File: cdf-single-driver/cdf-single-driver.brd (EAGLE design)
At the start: 48.3 x 40.6 mm, 30 parts, among them IC1 R-789.0-0.5, IC2 UCC27423

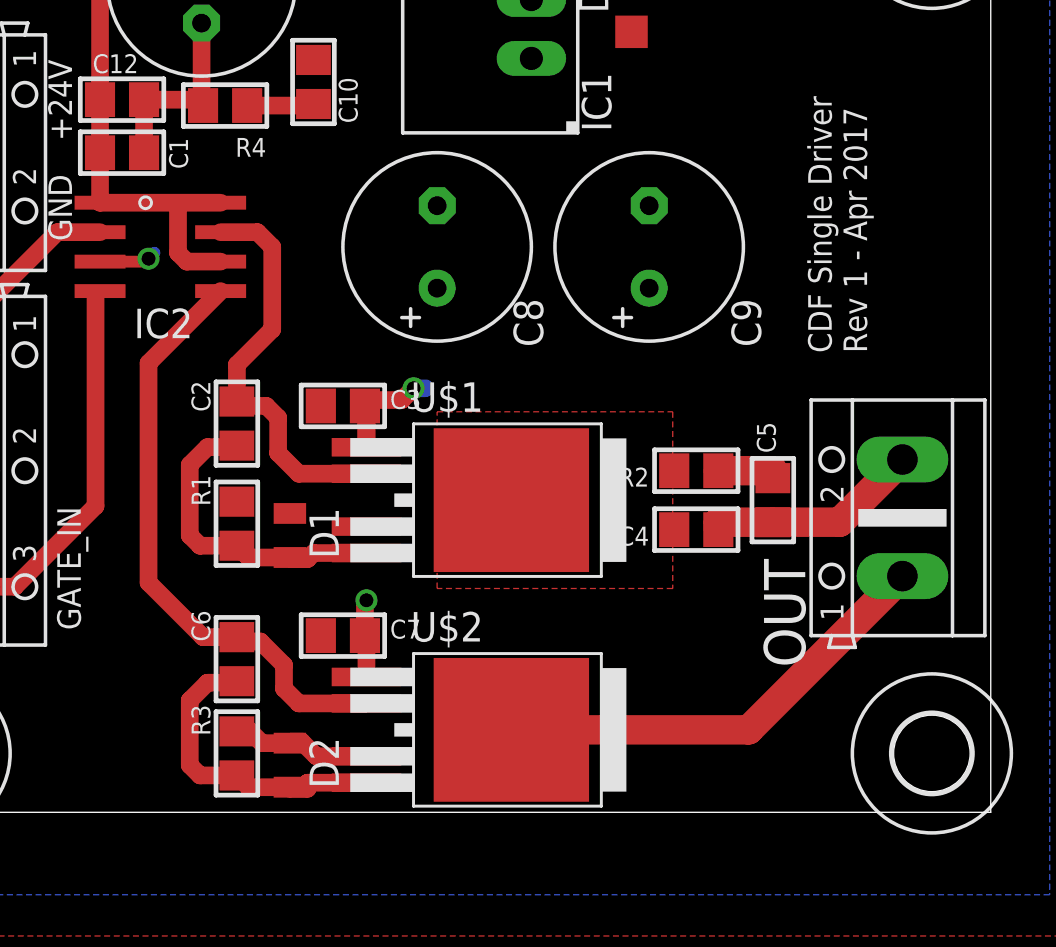
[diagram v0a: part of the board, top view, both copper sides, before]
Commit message: small cdf-single-driver changes
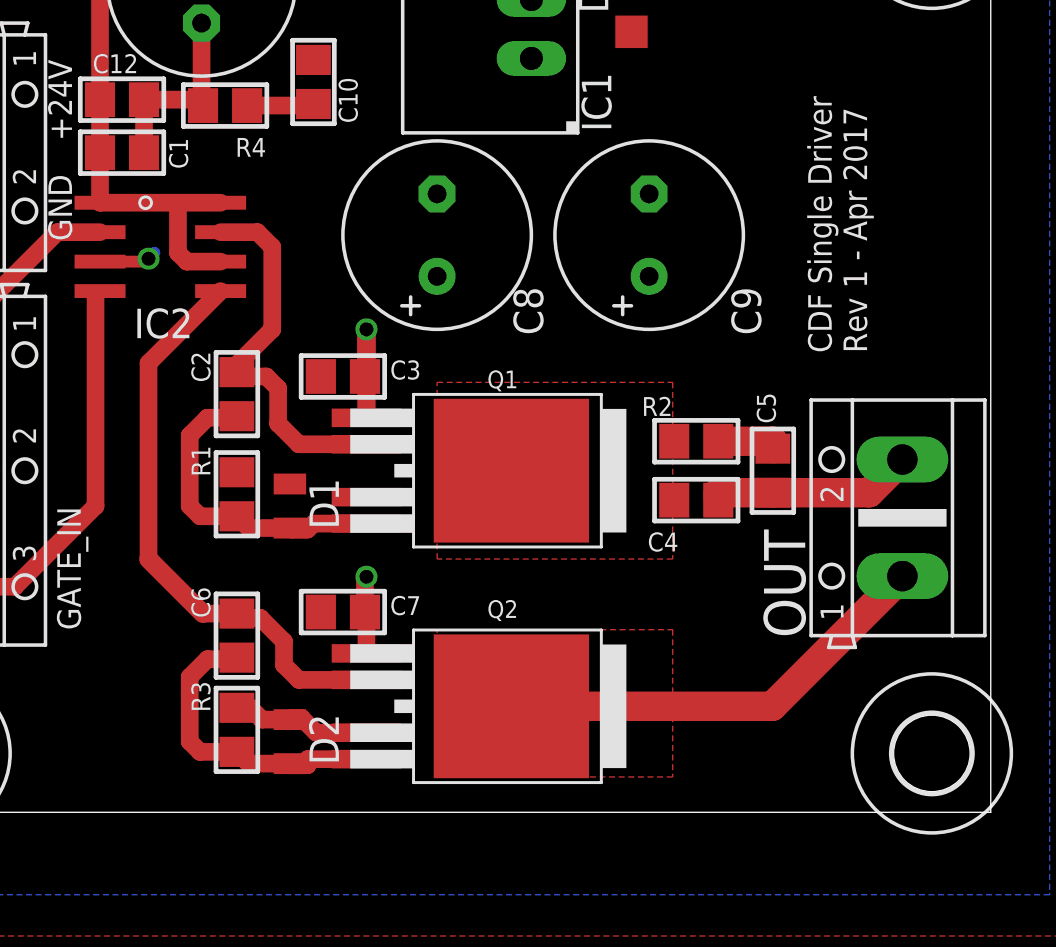
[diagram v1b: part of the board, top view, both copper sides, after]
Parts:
- removed U$1, U$2: FDD8424H, keves:TO252-4
- added Q1, Q2: FDD8424H, keves:TO252-4
- moved C2 1.27 mm to (15.7, 18.0)
- moved C3 1.27 mm to (20.3, 18.8)
- moved C4 1.27 mm to (35.6, 13.5)
- moved C5 1.27 mm to (38.9, 14.7)
- moved D1 1.27 mm to (18.0, 13.2)
- moved R1 1.27 mm to (15.7, 13.7)
- moved R2 1.27 mm to (35.6, 16.0)
- moved C6 1.02 mm to (15.7, 7.62)
- moved D2 1.02 mm to (18.0, 3.05)
- moved R3 1.02 mm to (15.7, 3.56)
- moved C7 1.02 mm to (20.3, 8.64)
- moved C8 0.51 mm to (24.4, 24.9)
- moved C9 0.51 mm to (33.5, 24.9)
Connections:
- net +24V: now also Q1.4, Q2.4; no longer U$1.4, U$2.4
- net GND: now also Q1.1, Q2.1; no longer U$1.1, U$2.1
- net N$10: now also Q2.TAB; no longer U$2.TAB
- net N$3: now also Q1.2; no longer U$1.2
- net N$4: now also Q1.5; no longer U$1.5
- net N$5: now also Q1.TAB; no longer U$1.TAB
- net N$8: now also Q2.2; no longer U$2.2
- net N$9: now also Q2.5; no longer U$2.5
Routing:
- net N$3: track 17.6 -> 16.3 mm
- net N$8: track 26.0 -> 25.0 mm
- net GND: track 20.9 -> 19.9 mm
- net N$7: track 9.38 -> 8.85 mm
- added copper zone on layer 1, net N$10

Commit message: wip
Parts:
- C1: value 1u -> 220u; device microbuilder:0805 -> rcl:E3,5-8
- C10, C3: device microbuilder:0805 -> rcl:C1210
- C11: value 330u (661-ELXZ250ELL331MH1) -> 2.2u; device rcl:E3,5-8 -> rcl:C1210
- C12, C6: value 0.1u -> 1u; device microbuilder:0805 -> microbuilder:1206
- C2: value 0.1u -> 220u; device microbuilder:0805 -> rcl:E3,5-8
- C4: value 2.2u -> 330u (661-ELXZ250ELL331MH1); device microbuilder:0805 -> rcl:E3,5-8
- C5: value 1u -> 0.1u
- C7: value 4.7u -> 0.1u
- C8: value 220u -> 0.1u; device rcl:E3,5-8 -> microbuilder:0805
- C9: value 220u -> 4.7u; device rcl:E3,5-8 -> rcl:C1210
- D1: value MCL4148-TR -> (none); device diode:MICROMELF-W -> diode:SOD123
- D3: value (none) -> MCL4148-TR; device diode:SOD123 -> diode:MICROMELF-W
- R1: value 1k -> 1
- R2: value 15 -> 1k
- R4: value 1 -> 15; device microbuilder:0805 -> rcl:R1210
- moved H2 55.9 mm to (45.7, 2.54)
- moved H3 55.9 mm to (2.54, 38.1)
- moved C12 33.0 mm to (39.4, 14.2), turned to 270 degrees
- moved C5 32.3 mm to (10.8, 30.7), turned to 0 degrees
- moved C4 30.9 mm to (14.2, 35.8), turned to 270 degrees
- moved C11 28.4 mm to (35.6, 17.0), turned to 0 degrees
- moved R4 26.9 mm to (35.8, 13.2), turned to 0 degrees
- moved D1 26.8 mm to (32.8, 35.6), turned to 90 degrees
- moved D3 26.8 mm to (18.0, 13.2), turned to 270 degrees
- moved R2 23.4 mm to (15.7, 3.56), turned to 90 degrees
- moved C1 23.0 mm to (33.5, 24.9), turned to 90 degrees
- moved C6 21.4 mm to (10.8, 28.4), turned to 180 degrees
- moved C9 20.4 mm to (20.6, 9.14), turned to 0 degrees
- moved R1 16.8 mm to (15.2, 30.5), turned to 180 degrees
- moved C10 12.0 mm to (20.6, 19.6), turned to 0 degrees
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- renumbered 24V to X1
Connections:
- net +24V: now also C1.+, C10.1, C2.+, C3.2, C9.1, R2.2; no longer C10.2, C3.1, C7.1, C8.+, C9.+, R1.2
- net +9V: now also C4.+, C5.1, C6.2, D1.A; no longer C1.2, C11.+, C12.1, D3.A
- net GND: now also C1.-, C10.2, C2.-, C4.-, C5.2, C6.1, C9.2, R1.2; no longer C1.1, C11.-, C12.2, C3.2, C7.2, C8.-, C9.-, R4.2
- net N$10: now also Q1.TAB; no longer Q2.TAB
- net N$11: now also C3.1, R1.1; no longer C10.1, R4.1
- net N$3: now also C8.2, Q2.2; no longer C2.2, Q1.2
- net N$4: now also C8.1, D3.A, Q2.5, R3.1; no longer C2.1, D1.A, Q1.5, R1.1
- net N$5: now also C11.1, Q2.TAB, R4.1; no longer C4.2, Q1.TAB, R2.2
- net N$6: now also C12.2, R4.2; no longer C5.2, R2.1
- net N$7: now also C11.2, C12.1; no longer C4.1, C5.1
- net N$8: now also C7.2, Q1.2; no longer C6.2, Q2.2
- net N$9: now also C7.1, Q1.5, R2.1; no longer C6.1, Q2.5, R3.1
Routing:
- net GND: track 19.9 -> 22.5 mm
- net N$10: track 19.9 -> 20.4 mm
